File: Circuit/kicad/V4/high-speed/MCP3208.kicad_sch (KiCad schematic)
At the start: 15 parts, among them J16 Conn_01x02_Pin, J17 Conn_01x02_Pin, J18 Conn_01x02_Pin, J19 Conn_01x02_Pin, J20 Conn_01x02_Pin, J21 Conn_01x02_Pin, U24 MCP3208

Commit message: kicad: high speed V2.2 Circuit finish psu bom update
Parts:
- removed J16, J17, J18, J19, J20, J21: Conn_01x02_Pin, Connector_PinHeader_2.54mm:PinHeader_2x01_P2.54mm_Vertical, symbol Connector:Conn_01x02_Pin
- added C50, C53: 1uf, Capacitor_SMD:C_0805_2012Metric, symbol Device:C
- added C54: 100nf, Capacitor_SMD:C_0805_2012Metric, symbol Device:C
- added C55: 22nf c0g, Capacitor_SMD:C_0805_2012Metric, symbol Device:C
- added R100, R102, R104, R106, R108, R111, R114, R117: 1K, Resistor_SMD:R_0805_2012Metric, symbol Device:R
- added R110, R113, R116: 10K ntc, Resistor_SMD:R_0805_2012Metric, symbol Device:R
- added R112, R115: 10K, Resistor_SMD:R_0805_2012Metric, symbol Device:R
- added R98: 10R, Resistor_SMD:R_0805_2012Metric, symbol Device:R
- added U25: XC6206P332MR, Package_TO_SOT_SMD:SOT-23-3, symbol Regulator_Linear:XC6206PxxxMR
- C51: renamed from C52; Cikkszám (none) -> 100.011.22; Link (none) -> https://www.hestore.hu/prod_10001122.html
- C52: renamed from C53; Cikkszám (none) -> 100.380.72; Link (none) -> https://www.hestore.hu/prod_10038072.html
- R101: renamed from R71; value 10k -> 10K; Cikkszám (none) -> 100.011.45; Link (none) -> https://www.hestore.hu/prod_10001145.html
- R103: renamed from R72; value 10k -> 10K; Cikkszám (none) -> 100.011.45; Link (none) -> https://www.hestore.hu/prod_10001145.html
- R105: renamed from R73; value 10k -> 10K; Cikkszám (none) -> 100.011.45; Link (none) -> https://www.hestore.hu/prod_10001145.html
- R107: renamed from R74; value 10k -> 10K; Cikkszám (none) -> 100.011.45; Link (none) -> https://www.hestore.hu/prod_10001145.html
- R109: renamed from R75; value 10k -> 10K; Cikkszám (none) -> 100.011.45; Link (none) -> https://www.hestore.hu/prod_10001145.html
- R99: renamed from R70; value 10k -> 10K; Cikkszám (none) -> 100.011.45; Link (none) -> https://www.hestore.hu/prod_10001145.html
- U26: renamed from U24; Cikkszám (none) -> 100.491.18; Link (none) -> https://www.hestore.hu/prod_10049118.html
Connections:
- net 3V3: now also C53.1, C54.1, C55.1, R112.1, R115.1; no longer C51.1, C52.2, U26.15 (Vref)
- net GND: now also C50.1, C53.2, C54.2, C55.2, R110.1, R113.1, R116.1, U25.1 (GND)
- net 0NTC: now reaches R101.2
- net 0NTC: now also R102.1
- net PSU-NTC: now reaches R99.2
- net PSU-NTC: now also R100.1
- net 3NTC: now reaches R107.2
- net 3NTC: now also R108.1
- net at U26.5 (CH4): now also R108.2
- net at R109.2: now also R110.2, R111.1
- net at U26.6 (CH5): now also R111.2
- net 1NTC: now reaches R103.2
- net 1NTC: now also R104.1
- net at U26.2 (CH1): now also R102.2
- net at U26.1 (CH0): now also R100.2
- net at U26.3 (CH2): now also R104.2
- net at U26.4 (CH3): now also R106.2
- net at U26.7 (CH6): now also R114.2
- net at U26.8 (CH7): now also R117.2
- net 2NTC: now reaches R105.2
- net 2NTC: now also R106.1
- new net: C50.2, C51.1, C52.2, R98.1, U26.15 (Vref)
- new net: R115.2, R116.2, R117.1
- new net: R98.2, U25.2 (VO)
- new net: R112.2, R113.2, R114.1
- new net 5v_to_ref: U25.3 (VI)
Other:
- moved on the sheet: C51, C52, R101, R103, R105, R107, R109, R99

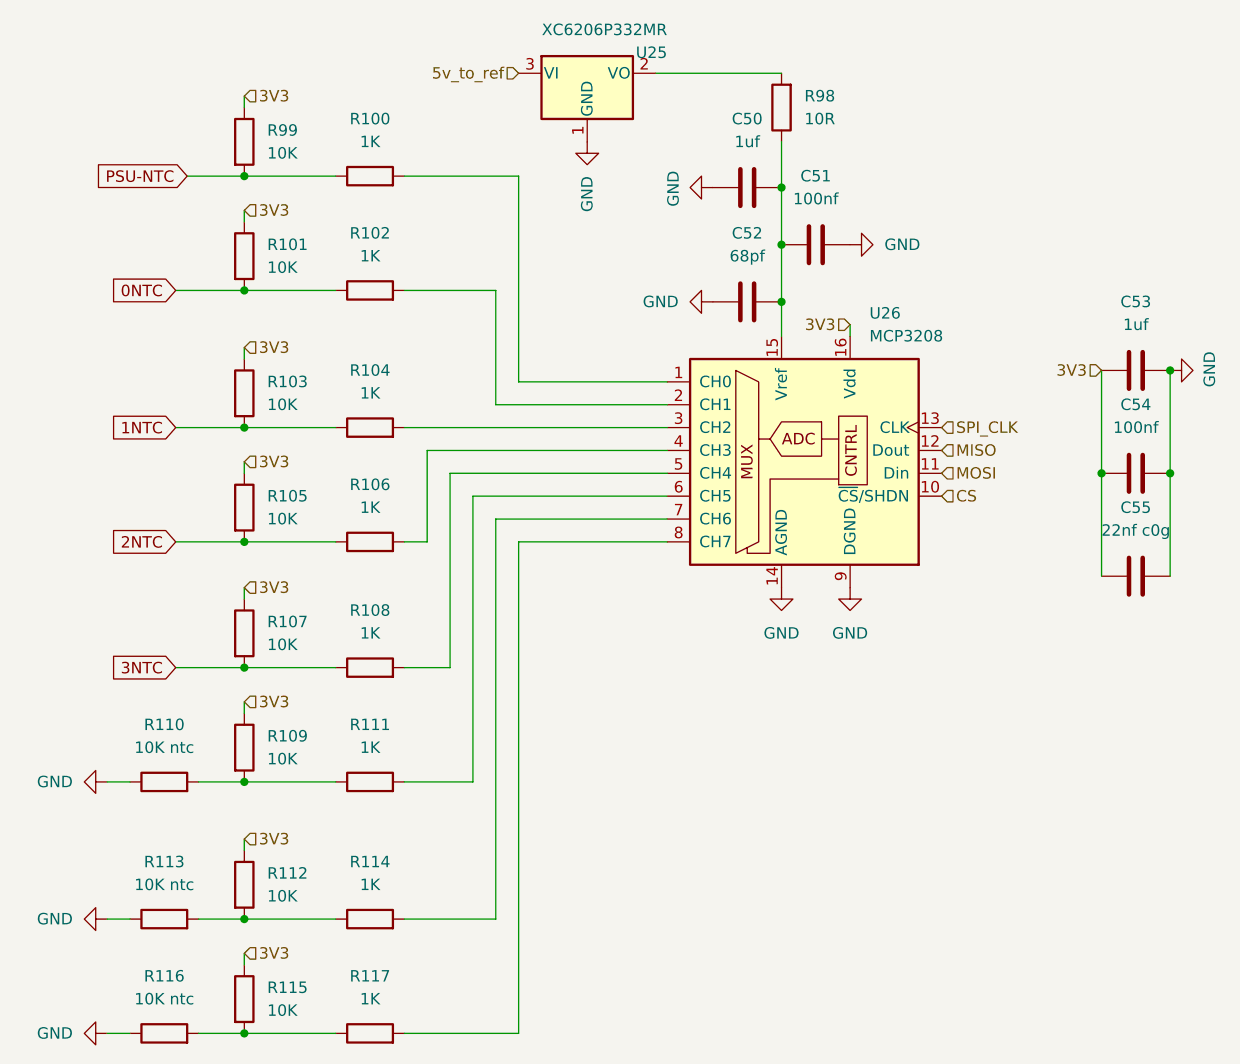
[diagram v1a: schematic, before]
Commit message: finished high-speed panel schematic and first try to doute gpios
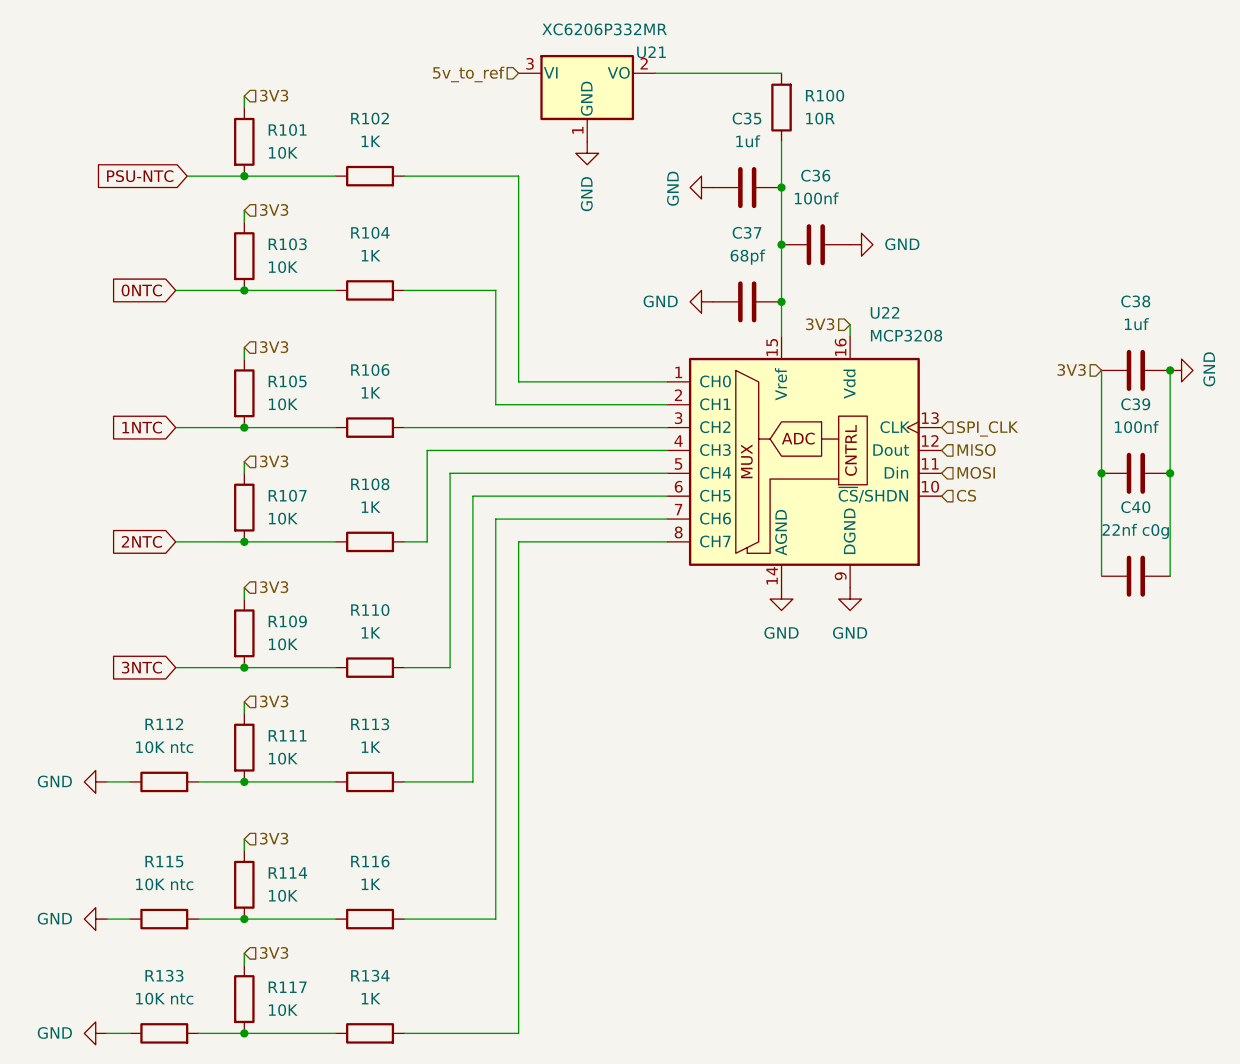
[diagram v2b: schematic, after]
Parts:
- renumbered C50 to C35, C51 to C36, C52 to C37, C53 to C38, C54 to C39, C55 to C40, R98 to R100, R99 to R101, R100 to R102, R101 to R103, R102 to R104, R103 to R105, R104 to R106, R105 to R107, R106 to R108, R107 to R109, R108 to R110, R109 to R111, R110 to R112, R111 to R113, R112 to R114, R113 to R115, R114 to R116, R115 to R117, R116 to R133, R117 to R134, U25 to U21, U26 to U22

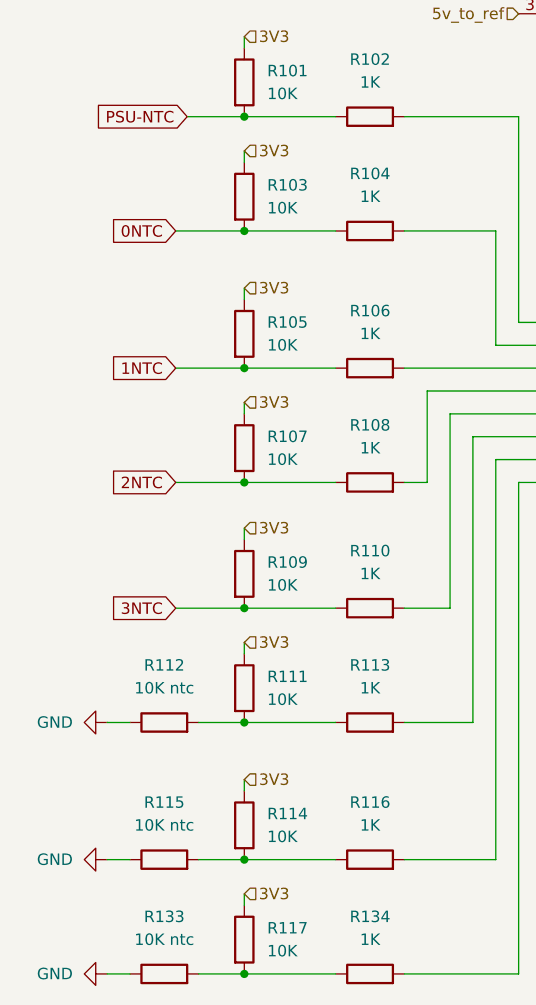
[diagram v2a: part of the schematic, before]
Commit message: High Speed all routed, DRC, DFM shows 0 error (without silkscreen layers)
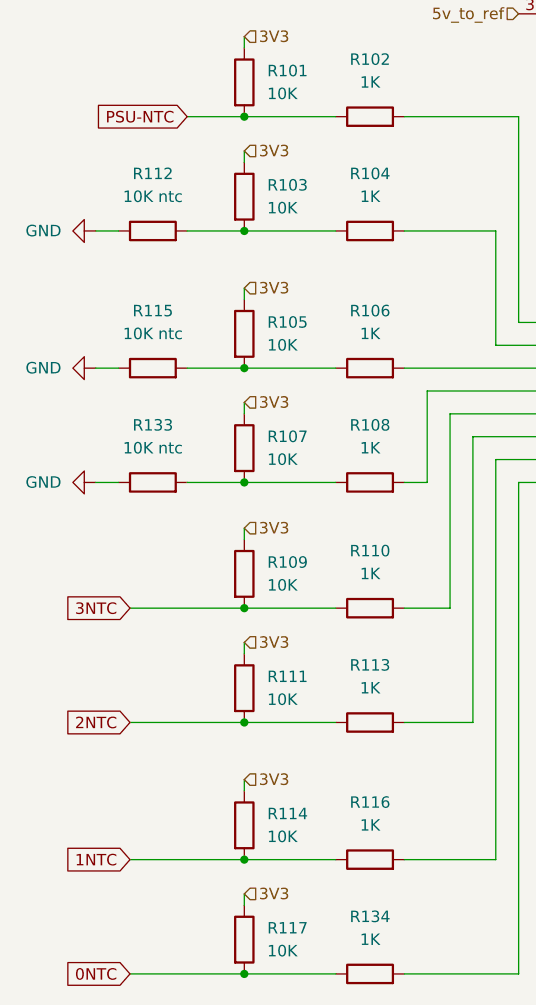
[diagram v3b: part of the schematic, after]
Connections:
- net 0NTC: now also R117.2, R134.1; no longer R103.2, R104.1
- net 1NTC: now also R114.2, R116.1; no longer R105.2, R106.1
- net 2NTC: now also R111.2, R113.1; no longer R107.2, R108.1
- new net: R103.2, R104.1, R112.2
- new net: R107.2, R108.1, R133.2
- new net: R105.2, R106.1, R115.2
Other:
- moved on the sheet: R112, R115, R133
